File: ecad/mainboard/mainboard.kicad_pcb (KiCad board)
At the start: 4 copper layers, 301.3 x 160 mm, 116 parts, among them J1 TYPE-C-31-M-12, J2 SWD, K0 DRV5056A3xQDBZxR, K1 DRV5056A3xQDBZxR, K10 DRV5056A3xQDBZxR, K11 DRV5056A3xQDBZxR, K12 DRV5056A3xQDBZxR, K13 DRV5056A3xQDBZxR, K14 DRV5056A3xQDBZxR, K15 DRV5056A3xQDBZxR, K2 DRV5056A3xQDBZxR, K3 DRV5056A3xQDBZxR, K4 DRV5056A3xQDBZxR, K5 DRV5056A3xQDBZxR, K6 DRV5056A3xQDBZxR, K7 DRV5056A3xQDBZxR, K8 DRV5056A3xQDBZxR, K9 DRV5056A3xQDBZxR, SW3 SW_Push, SW4 SW_Push, U1 NCP1117ST33T3G, U2 USBLC6-2SC6, U22 CD4051BM96, U23 CD4051BM96, U3 W25Q128JVS, U5 RP2040, Y1 ABM8-272-T3

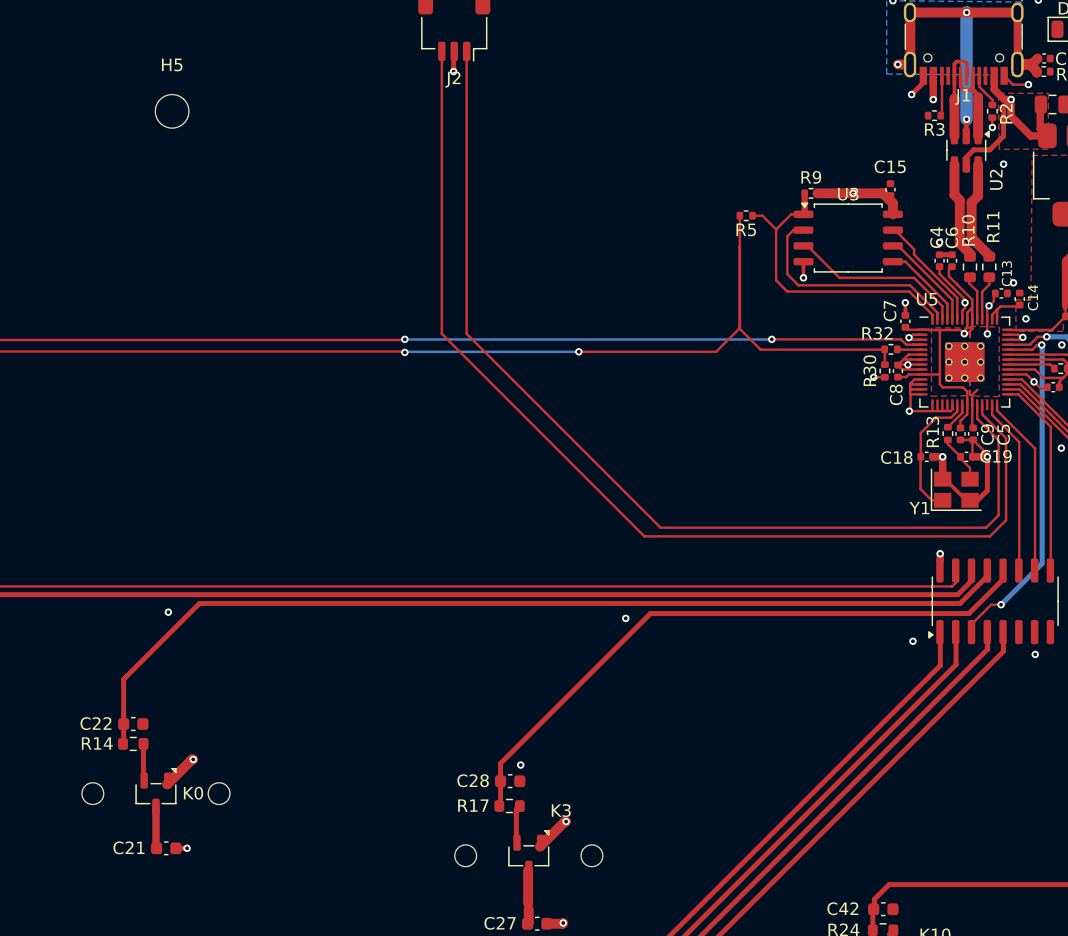
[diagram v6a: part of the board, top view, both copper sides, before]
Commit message: Python script to update switch positions
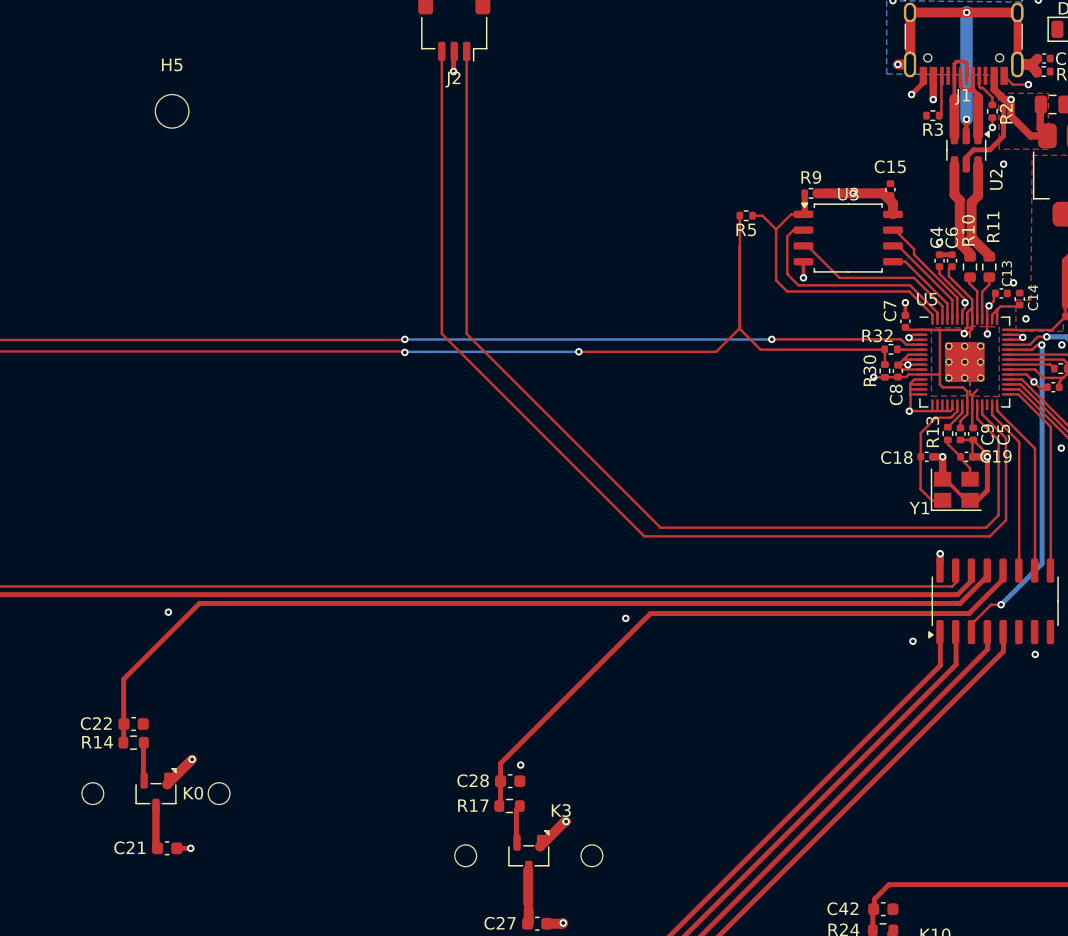
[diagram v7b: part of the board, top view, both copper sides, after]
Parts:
- moved R3 0.13 mm to (207.5, 50.5)
- moved R14 0.10 mm to (143.2, 100.9)
- moved C21 0.08 mm to (145.9, 109.4)
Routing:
- net +3.3V: track 129.0 -> 130.2 mm
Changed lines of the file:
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@@
 		(tags "resistor")
 		(property "Reference" "R32"
-			(at 1.09 1.25 0)
+			(at 1.09 1.05 0)
 			(layer "F.SilkS")
 			(effects
@@
 	(footprint "Resistor_SMD:R_0402_1005Metric"
 		(layer "F.Cu")
-		(at 207.64 50.45)
+		(at 207.51 50.45)
 		(descr "Resistor SMD 0402 (1005 Metric), square (rectangular) end terminal, IPC_7351 nominal, (Body size source: IPC-SM-782 page 72, https://www.pcb-3d.com/wordpress/wp-content/uploads/ipc-sm-782a_amendment_1_and_2.pdf), generated with kicad-footprint-generator")
 		(tags "resistor")
@@
 			)
 		)
-		(property "フィールド5" ""
+		(property "フィールド6" ""
 			(at 0 0 0)
 			(unlocked yes)
@@
 			)
 		)
-		(property "フィールド6" ""
+		(property "DigitalSwitch" "K12"
 			(at 0 0 0)
 			(unlocked yes)
@@
 	(footprint "Resistor_SMD:R_0603_1608Metric"
 		(layer "F.Cu")
-		(at 143.175 101 180)
+		(at 143.2 100.9 180)
 		(descr "Resistor SMD 0603 (1608 Metric), square (rectangular) end terminal, IPC_7351 nominal, (Body size source: IPC-SM-782 page 72, https://www.pcb-3d.com/wordpress/wp-content/uploads/ipc-sm-782a_amendment_1_and_2.pdf), generated with kicad-footprint-generator")
 		(tags "resistor")
@@
 			)
 		)
-		(property "フィールド5" ""
+		(property "フィールド6" ""
 			(at 0 0 0)
 			(unlocked yes)
@@
 			)
 		)
-		(property "フィールド6" ""
+		(property "DigitalSwitch" "K14"
 			(at 0 0 0)
 			(unlocked yes)
@@
 		)
 		(property "Value" "10k"
-			(at 0 1.17 90)
+			(at -4.21 0.95 90)
 			(layer "F.Fab")
 			(effects
@@
 			)
 		)
-		(property "フィールド5" ""
+		(property "フィールド6" ""
 			(at 0 0 0)
 			(unlocked yes)
@@
 			)
 		)
-		(property "フィールド6" ""
+		(property "DigitalSwitch" "K5"
 			(at 0 0 0)
 			(unlocked yes)
@@
 			)
 		)
-		(property "フィールド5" ""
+		(property "フィールド6" ""
 			(at 0 0 0)
 			(unlocked yes)
@@
 			)
 		)
-		(property "フィールド6" ""
+		(property "DigitalSwitch" "K8"
 			(at 0 0 0)
 			(unlocked yes)
@@
 			)
 		)
-		(property "フィールド5" ""
+		(property "フィールド6" ""
 			(at 0 0 0)
 			(unlocked yes)
@@
 			)
 		)
-		(property "フィールド6" ""
+		(property "DigitalSwitch" "K7"
 			(at 0 0 0)
 			(unlocked yes)
@@
 			)
 		)
-		(property "フィールド5" ""
+		(property "フィールド6" ""
 			(at 0 0 0)
 			(unlocked yes)
@@
 			)
 		)
-		(property "フィールド6" ""
+		(property "DigitalSwitch" "K13"
 			(at 0 0 0)
 			(unlocked yes)
@@
 			)
 		)
-		(property "フィールド5" ""
-			(at 0 0 0)
-			(unlocked yes)
-			(layer "F.Fab")
-			(hide yes)
-			(effects
-				(font
-					(size 1 1)
-					(thickness 0.15)
-				)
-			)
-		)
-		(property "フィールド6" ""
+		(property "DigitalSwitch" "K1"
 			(at 0 0 0)
 			(unlocked yes)
@@
 			)
 		)
-		(property "フィールド5" ""
+		(property "フィールド6" ""
 			(at 0 0 0)
 			(unlocked yes)
@@
 			)
 		)
-		(property "フィールド6" ""
+		(property "DigitalSwitch" "K4"
 			(at 0 0 0)
 			(unlocked yes)
@@
 			)
 		)
-		(property "フィールド5" ""
+		(property "フィールド6" ""
 			(at 0 0 0)
 			(unlocked yes)
@@
 			)
 		)
-		(property "フィールド6" ""
+		(property "DigitalSwitch" "K6"
 			(at 0 0 0)
 			(unlocked yes)
@@
 	(footprint "Capacitor_SMD:C_0603_1608Metric"
 		(layer "F.Cu")
-		(at 145.825 109.4)
+		(at 145.9 109.4)
 		(descr "Capacitor SMD 0603 (1608 Metric), square (rectangular) end terminal, IPC_7351 nominal, (Body size source: IPC-SM-782 page 76, https://www.pcb-3d.com/wordpress/wp-content/uploads/ipc-sm-782a_amendment_1_and_2.pdf), generated with kicad-footprint-generator")
 		(tags "capacitor")
@@
 			)
 		)
-		(property "フィールド5" ""
+		(property "フィールド6" ""
 			(at 0 0 0)
 			(unlocked yes)
@@
 			)
 		)
-		(property "フィールド6" ""
+		(property "DigitalSwitch" "K10"
 			(at 0 0 0)
 			(unlocked yes)
@@
 			)
 		)
-		(property "フィールド5" ""
+		(property "フィールド6" ""
 			(at 0 0 0)
 			(unlocked yes)
@@
 			)
 		)
-		(property "フィールド6" ""
+		(property "DigitalSwitch" "K2"
 			(at 0 0 0)
 			(unlocked yes)
@@
 			)
 		)
-		(property "フィールド5" ""
+		(property "フィールド6" ""
 			(at 0 0 0)
 			(unlocked yes)
@@
 			)
 		)
-		(property "フィールド6" ""
+		(property "DigitalSwitch" "K15"
 			(at 0 0 0)
 			(unlocked yes)
@@
 			)
 		)
-		(property "フィールド5" ""
+		(property "フィールド6" ""
 			(at 0 0 0)
 			(unlocked yes)
@@
 			)
 		)
-		(property "フィールド6" ""
+		(property "DigitalSwitch" "K9"
 			(at 0 0 0)
 			(unlocked yes)
@@
 			)
 		)
-		(property "フィールド5" ""
+		(property "フィールド6" ""
 			(at 0 0 0)
 			(unlocked yes)
@@
 			)
 		)
-		(property "フィールド6" ""
+		(property "DigitalSwitch" "K3"
 			(at 0 0 0)
 			(unlocked yes)
@@
 			)
 		)
-		(property "フィールド5" ""
+		(property "フィールド6" ""
 			(at 0 0 0)
 			(unlocked yes)
@@
 			)
 		)
-		(property "フィールド6" ""
+		(property "DigitalSwitch" "K0"
 			(at 0 0 0)
 			(unlocked yes)
@@
 	(footprint "Capacitor_SMD:C_0603_1608Metric"
 		(layer "F.Cu")
-		(at 143.175 99.4 180)
+		(at 143.2 99.4 180)
 		(descr "Capacitor SMD 0603 (1608 Metric), square (rectangular) end terminal, IPC_7351 nominal, (Body size source: IPC-SM-782 page 76, https://www.pcb-3d.com/wordpress/wp-content/uploads/ipc-sm-782a_amendment_1_and_2.pdf), generated with kicad-footprint-generator")
 		(tags "capacitor")
@@
 			)
 		)
-		(property "フィールド5" ""
+		(property "フィールド6" ""
 			(at 1.58 0.025 0)
 			(unlocked yes)
@@
 			)
 		)
-		(property "フィールド6" ""
-			(at 1.58 0.025 0)
+		(property "DigitalSwitch" "K11"
+			(at 0 0 0)
 			(unlocked yes)
 			(layer "F.Fab")
@@
 	)
 	(segment
-		(start 144.945 109.38)
-		(end 145 109.325)
-		(width 0.6)
-		(layer "F.Cu")
-		(net 2)
-	)
-	(segment
 		(start 206.6425 70.074)
 		(end 205.756 70.074)
@@
 	)
 	(segment
-		(start 145.895 104.2625)
-		(end 147.9075 102.25)
-		(width 0.8)
-		(layer "F.Cu")
-		(net 3)
-	)
-	(segment
 		(start 280.95 76.71)
 		(end 280.95 76.7625)
@@
 	)
 	(segment
+		(start 147.8 109.4)
+		(end 146.475 109.4)
+		(width 0.4)
+		(layer "F.Cu")
+		(net 3)
+	)
+	(segment
 		(start 215.051817 71.274)
 		(end 213.5175 71.274)
@@
 	)
 	(segment
+		(start 203.65 71.5)
+		(end 204.68 71.5)
+		(width 0.2)
+		(layer "F.Cu")
+		(net 3)
+	)
+	(segment
 		(start 212.28 66.8365)
 		(end 212.28 66.47)
@@
 	)
 	(segment
-		(start 147.9075 102.25)
-		(end 148 102.25)
-		(width 0.8)
-		(layer "F.Cu")
-		(net 3)
-	)
-	(segment
 		(start 282.75 112.86)
 		(end 282.79 112.82)
@@
 	)
 	(segment
+		(start 147.9075 102.25)
+		(end 145.895 104.2625)
+		(width 0.8)
+		(layer "F.Cu")
+		(net 3)
+	)
+	(segment
 		(start 201.1 56.7)
 		(end 203.5 56.7)
@@
 	)
 	(segment
-		(start 147.5 109.4)
-		(end 146.475 109.4)
-		(width 0.4)
-		(layer "F.Cu")
-		(net 3)
-	)
-	(segment
 		(start 176.455 115.47)
 		(end 177.71 115.47)
@@
 	)
 	(segment
+		(start 204.68 71.5)
+		(end 204.7 71.48)
+		(width 0.2)
+		(layer "F.Cu")
+		(net 3)
+	)
+	(segment
 		(start 219.03 54.02)
 		(end 219.03 58.376)
@@
 	)
 	(via
-		(at 148 102.25)
+		(at 147.9075 102.25)
 		(size 0.6)
 		(drill 0.3)
@@
 	)
 	(via
-		(at 147.5 109.4)
+		(at 147.8 109.4)
 		(size 0.6)
 		(drill 0.3)
@@
 	)
 	(segment
-		(start 208.244 50.366)
-		(end 208.06 50.55)
+		(start 208.2 47.289)
+		(end 208.2 50.41)
 		(width 0.20574)
 		(layer "F.Cu")
@@
 	(segment
 		(start 208.244 47.245)
-		(end 208.244 50.366)
+		(end 208.2 47.289)
+		(width 0.20574)
+		(layer "F.Cu")
+		(net 25)
+	)
+	(segment
+		(start 208.2 50.41)
+		(end 208.06 50.55)
 		(width 0.20574)
 		(layer "F.Cu")
@@
 	)
 	(segment
-		(start 211.244 48.126702)
-		(end 212.3 49.182702)
+		(start 211.244 47.245)
+		(end 211.244 48.12574)
 		(width 0.20574)
 		(layer "F.Cu")
@@
 	)
 	(segment
-		(start 211.244 47.245)
-		(end 211.244 48.126702)
+		(start 211.34113 48.22287)
+		(end 211.540994 48.22287)
 		(width 0.20574)
 		(layer "F.Cu")
@@
 	)
 	(segment
-		(start 212.3 49.182702)
+		(start 211.540994 48.22287)
+		(end 212.3 48.981876)
+		(width 0.20574)
+		(layer "F.Cu")
+		(net 30)
+	)
+	(segment
+		(start 212.3 48.981876)
 		(end 212.3 49.6)
 		(width 0.20574)
 		(layer "F.Cu")
+		(net 30)
+	)
+	(segment
+		(start 211.244 48.12574)
+		(end 211.34113 48.22287)
+		(width 0.20574)
+		(layer "F.Cu")

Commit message: Place all buttons
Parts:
- removed H10, H6, H7, H8, H9: MountingHole, MountingHole:MountingHole_2.7mm_M2.5
- H1, H2, H3, H4, H5: value MountingHole -> MountingHole_Pad; footprint MountingHole:MountingHole_2.7mm_M2.5 -> MountingHole:MountingHole_2.7mm_M2.5_Pad_Via
- moved H2 241.9 mm to (280.0, 70.0)
- moved H4 237.1 mm to (140.0, 160.0)
- moved H5 173.1 mm to (280.0, 160.0)
- moved H3 154.4 mm to (210.0, 125.0)
- moved H1 72.8 mm to (140.0, 70.0)
- moved J2 15.6 mm to (184.6, 43.2)
- moved C44 14.9 mm to (283.8, 85.4), turned to 0 degrees
- moved R25 14.4 mm to (283.8, 86.9), turned to 0 degrees
- moved C33 13.7 mm to (116.0, 134.4)
- moved R19 13.3 mm to (179.8, 126.9), turned to 0 degrees
- moved C23 13.3 mm to (116.0, 102.4)
- moved C31 13.2 mm to (176.0, 134.4)
- moved R20 13.2 mm to (119.8, 126.9), turned to 0 degrees
- moved C27 13.1 mm to (176.0, 102.4)
- moved C32 13.0 mm to (179.8, 125.4), turned to 0 degrees
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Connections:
- J2 pad MP: unconnected-(J2-MountPin-PadMP) -> (no net)
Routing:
- net DS_0_IN: track 126.0 -> 105.3 mm
- net BOOTSEL_SW: track 163.1 -> 143.2 mm
- net AS6: track 124.5 -> 106.3 mm
- net AS10: track 47.5 -> 29.4 mm
- net AS5: track 66.9 -> 49.1 mm
- net SWCLK: track 81.7 -> 64.8 mm
- net SWD: track 85.1 -> 68.8 mm
- net +3.3V: track 130.2 -> 144.5 mm, vias 41 -> 25
- net AS7: track 91.0 -> 76.7 mm
- net AS1: track 108.4 -> 94.8 mm
- net AS0: track 77.7 -> 64.5 mm
- net AS3: track 49.9 -> 36.9 mm
- net AS15: track 58.3 -> 70.4 mm
- net AS4: track 150.9 -> 139.1 mm
- net AS8: track 144.6 -> 137.6 mm
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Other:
- board size 301.3 x 160 mm -> 280 x 150 mm
